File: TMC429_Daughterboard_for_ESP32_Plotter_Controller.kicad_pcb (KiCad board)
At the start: 2 copper layers, 69.3 x 55.8 mm, 21 parts, among them J1 X Stepper A, J10 Y Limit, J11 X Limit, J2 X Stepper B, J3 X Stepper C, J4 Y Stepper A, J5 Y Stepper B, J6 Y Stepper C, J7 Z Motor, J8 Z_Diag, J9 Z Limit, U1 TMC2130, U2 TMC2130, U3 TMC429-BOB, U4 TMC2130

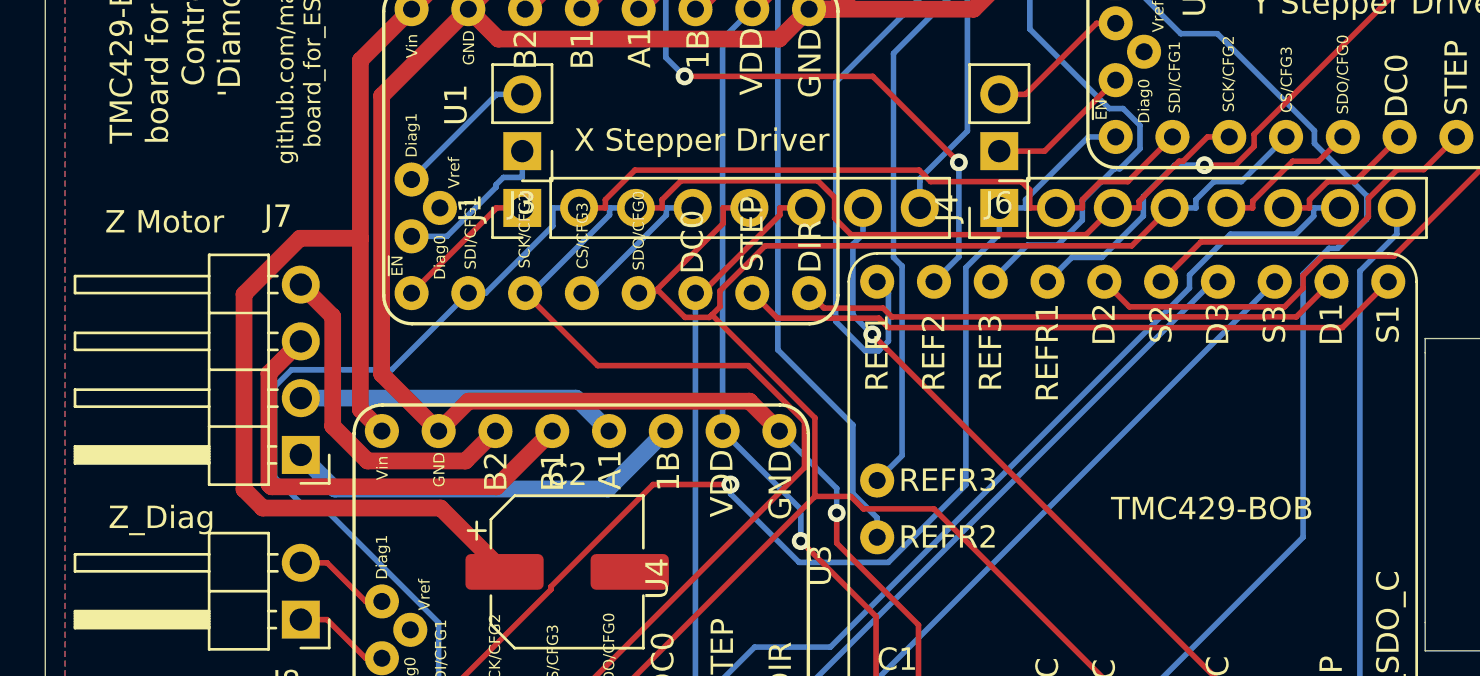
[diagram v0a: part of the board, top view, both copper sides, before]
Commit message: Fix MISO/CS pins
Moved MISO to correct pin and updated Schematic and PCB.
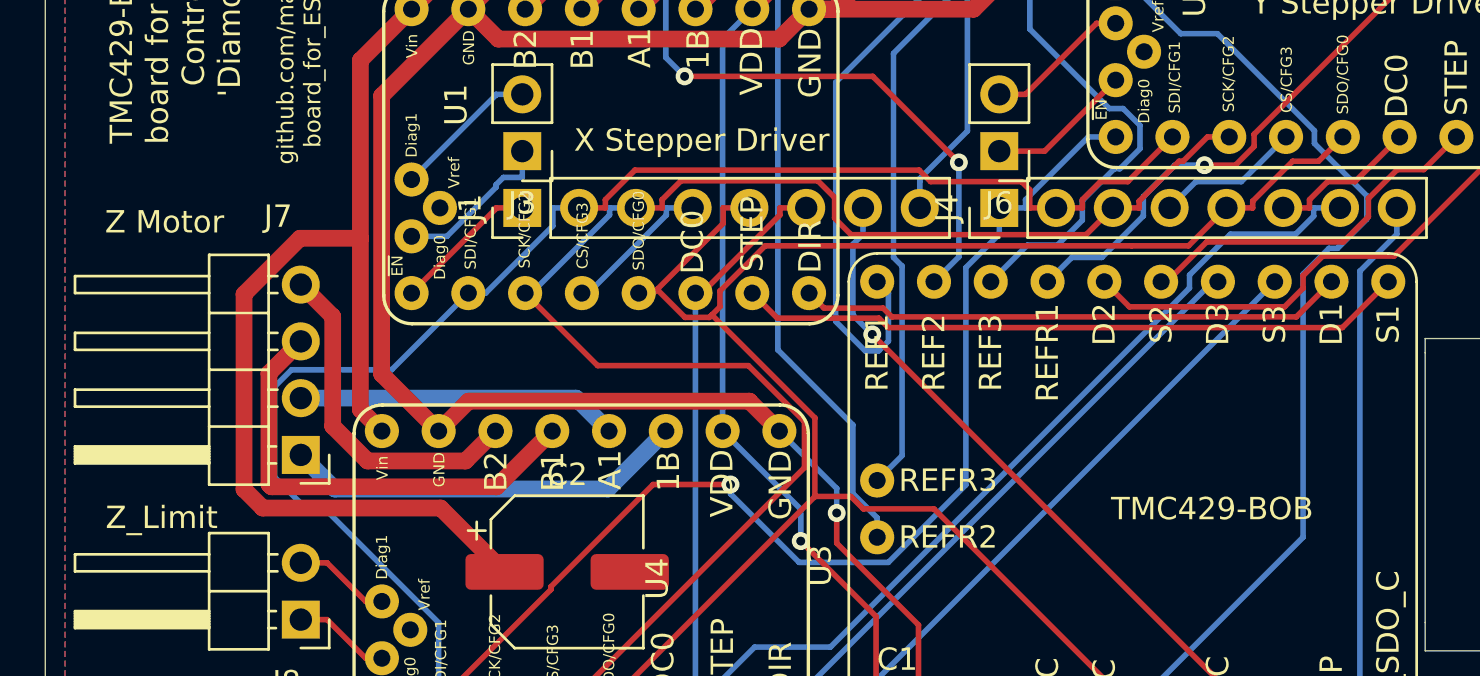
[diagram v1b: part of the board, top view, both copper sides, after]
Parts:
- J8: value Z_Diag -> Z_Limit
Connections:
- J4 pad 4: /MISO -> Net-(J4-Pad4)
- J4 pad 5: Net-(J4-Pad5) -> /MISO
- U2 pad 4: /MISO -> Net-(J4-Pad4)
- U2 pad 5: Net-(J4-Pad5) -> /MISO
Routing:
- net Net-(J4-Pad5): track 6.70 -> 0.00 mm
- net Net-(J4-Pad4): track 0.00 -> 6.52 mm
- net /MISO: track 86.7 -> 89.2 mm
